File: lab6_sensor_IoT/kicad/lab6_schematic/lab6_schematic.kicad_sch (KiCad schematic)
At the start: 6 parts, among them J1 NUCLEO-L432KC, J2 Conn_01x01, U1 DS1722

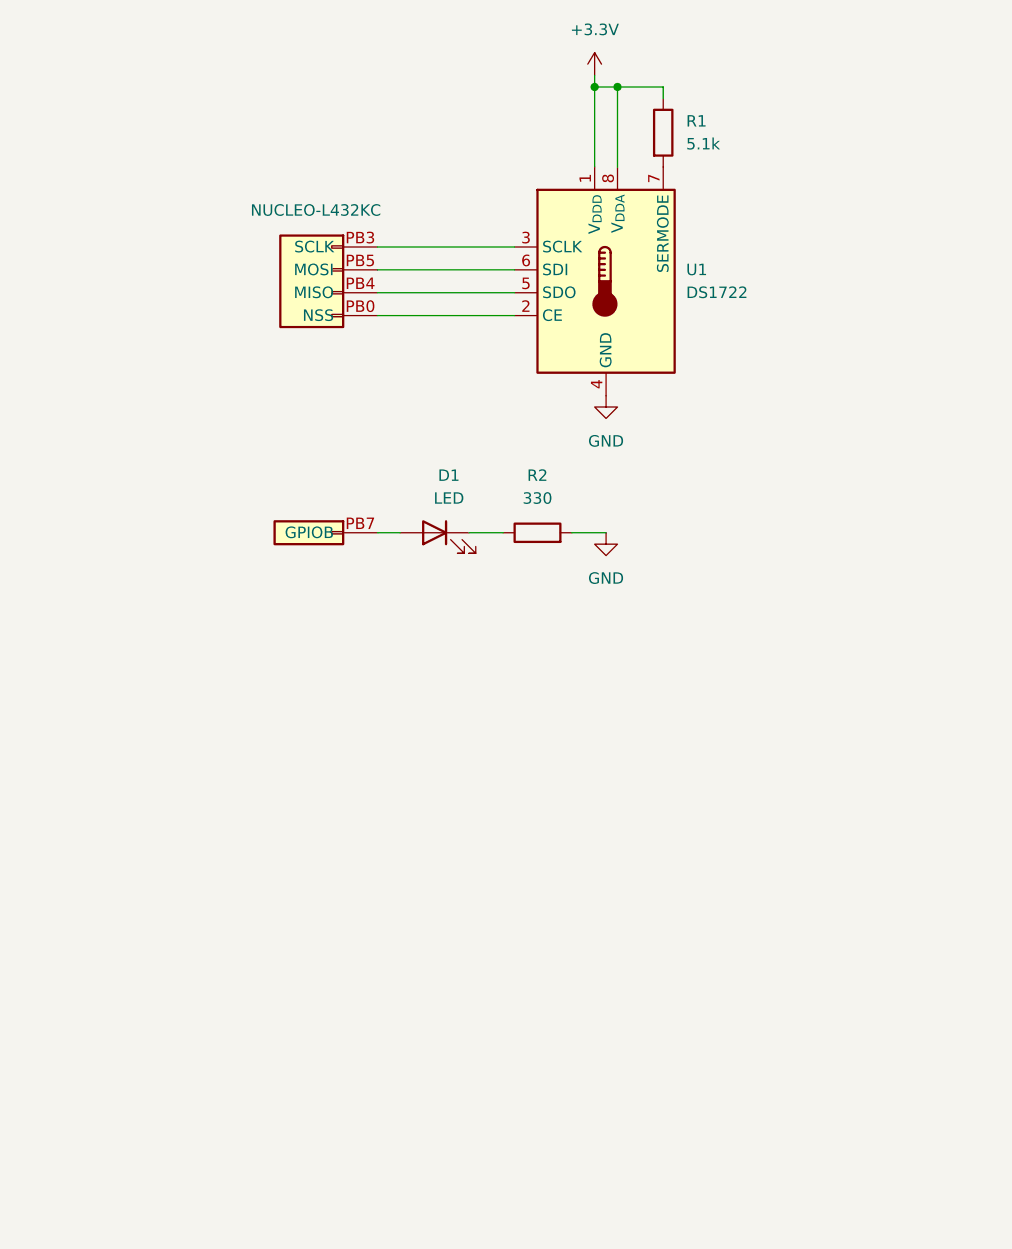
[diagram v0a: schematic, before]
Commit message: Cleaning up code from a couple different labs
For redos
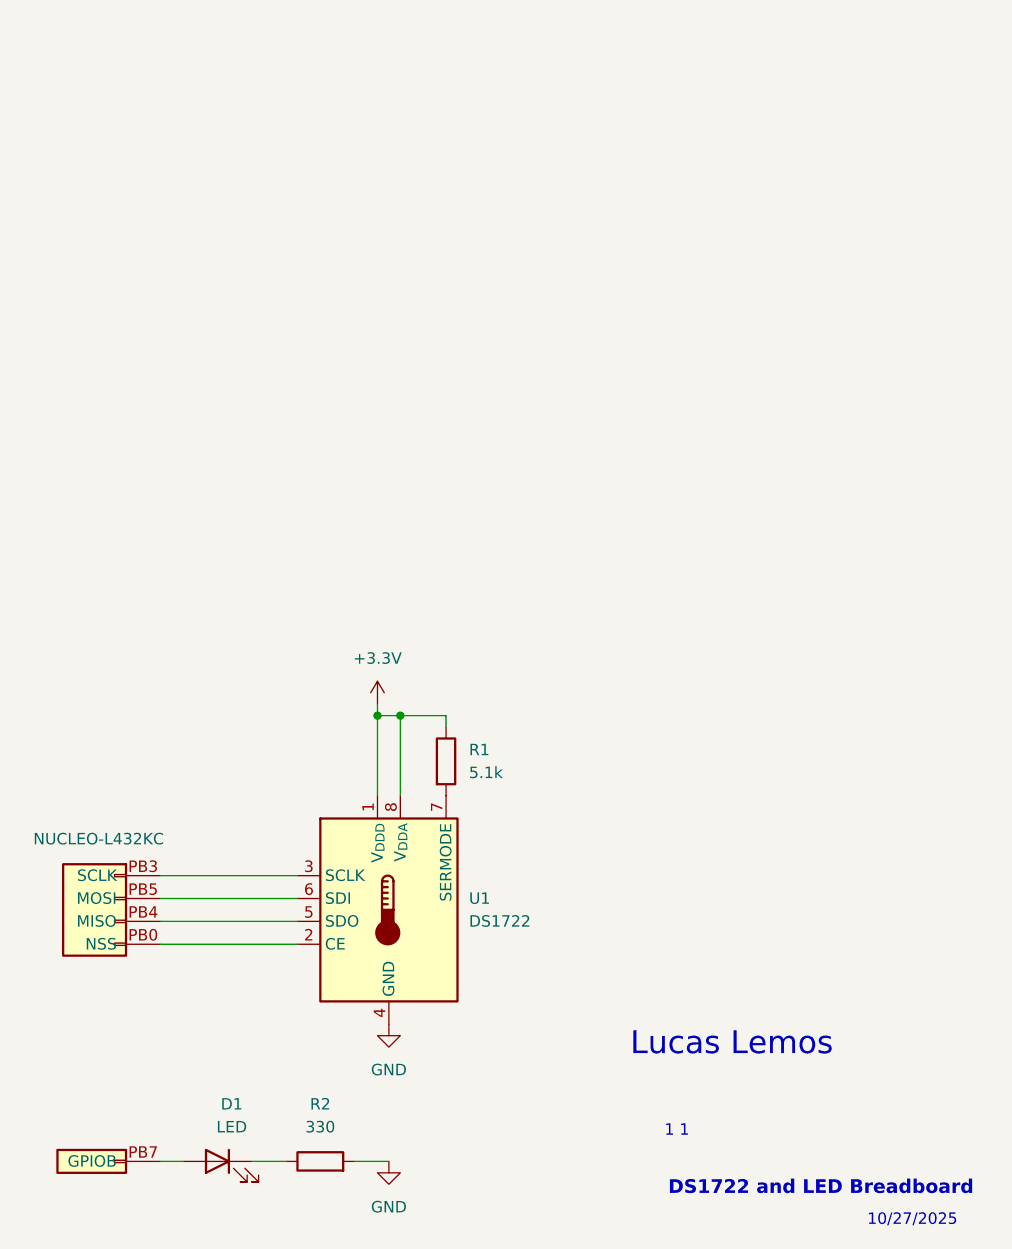
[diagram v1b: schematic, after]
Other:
- note added: "1 1"
- note added: "10/27/2025"
- note added: "DS1722 and LED Breadboard"
- note added: "Lucas Lemos"
- moved on the sheet: D1, R1, R2, U1
